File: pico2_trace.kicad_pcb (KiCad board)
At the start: 2 copper layers, 110 x 78 mm, 57 parts, among them J1B BREAKOUT, J2B BREAKOUT, J3 MIPI-20, J4 JST-SH-3 DEBUG, J5 USB-A HOST, J6 CORTEX-10, J7 JST-SH-3 DEBUG_PROBE, J8 USB-MICROB PWR, J9 USB-MICROB DEV, SW1 RESET

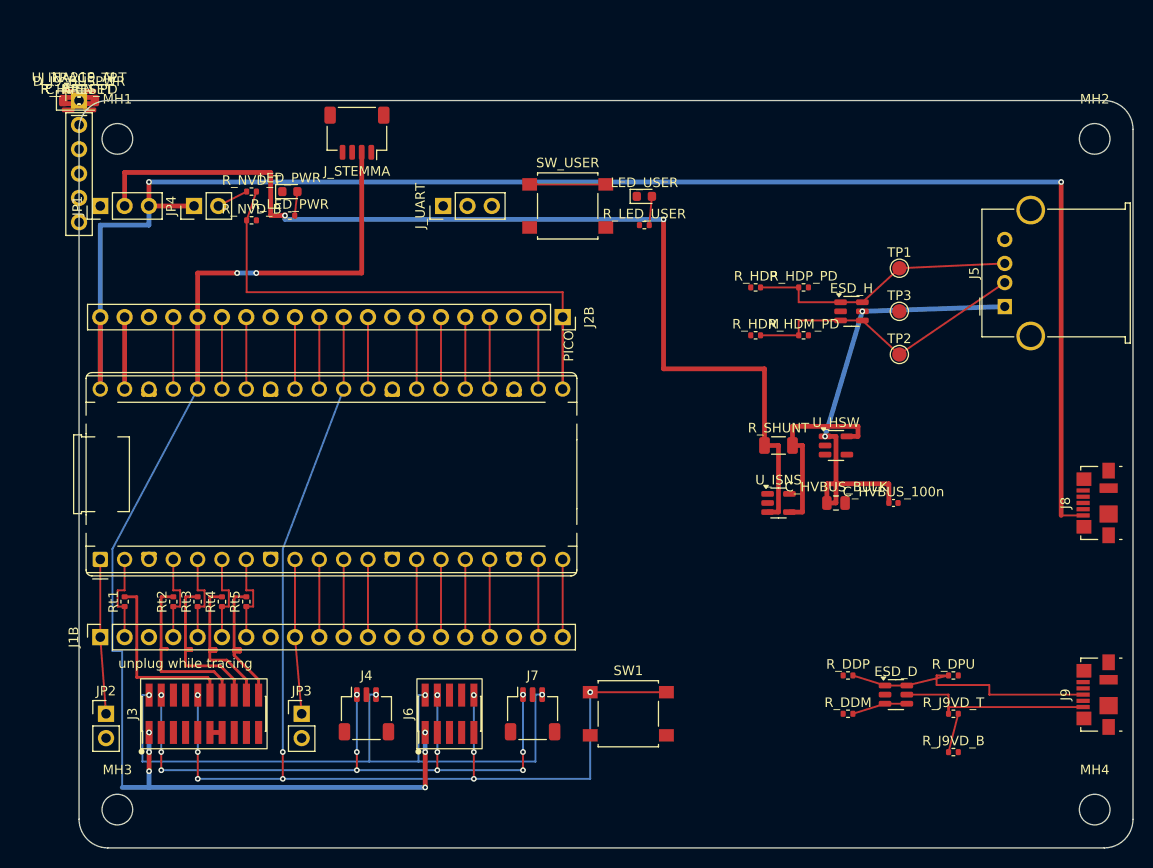
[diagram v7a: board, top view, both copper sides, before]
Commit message: WIP(14c): compact to 92x64, co-designed placement, routing rewrite
Gates NOT verified/green: silk noise 80 (target ~35), J_TRACE_TP removal
pending, full gate battery unrun. Preserved because the placement ordering
and route_trace.py band/corridor structure are reusable by the SMT-footprint
re-layout (Task 14e). Non-GND unconnected had reached 0 before the pass ended.
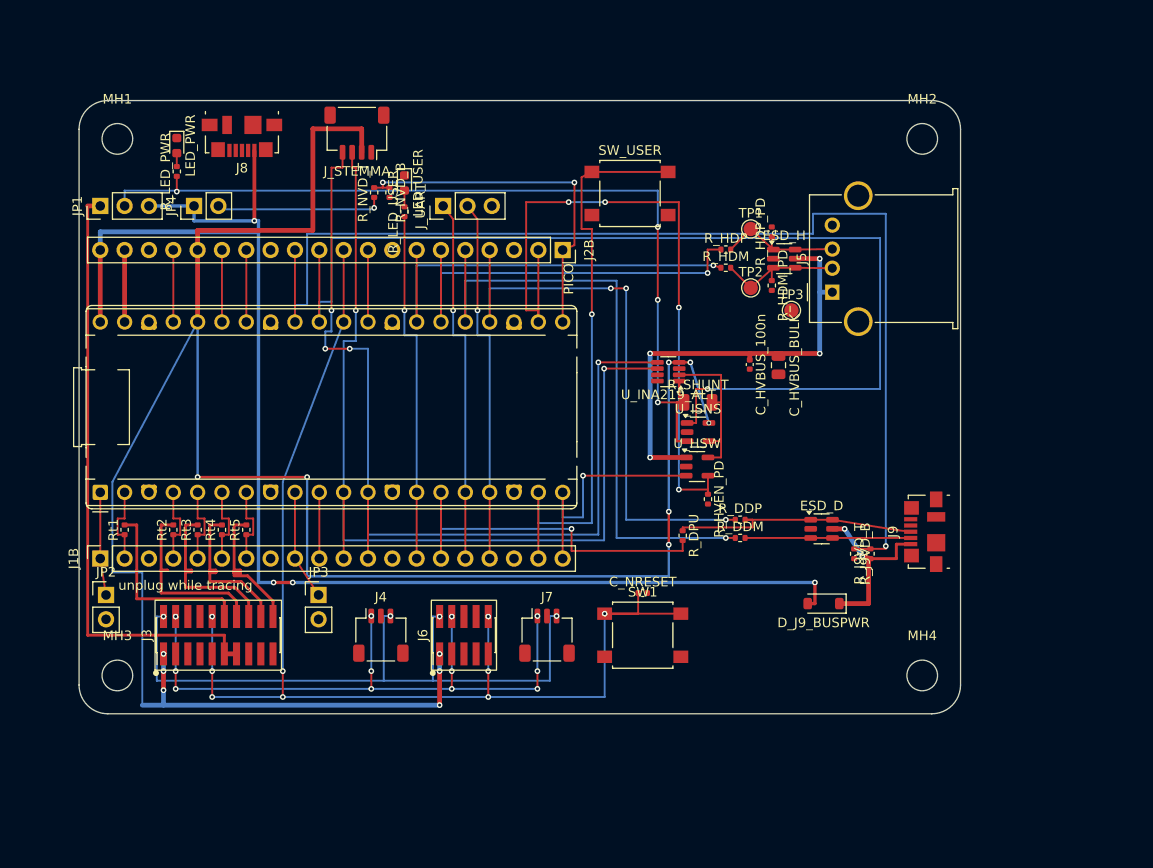
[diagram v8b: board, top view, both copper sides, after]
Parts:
- removed J_TRACE_TP: TRACE_TP, PinHeader_1x06_P2.54mm_Vertical
- moved J8 97.1 mm to (17.0, 3.75), turned to 180 degrees
- moved D_J9_BUSPWR 93.8 mm to (77.7, 52.5), turned to 180 degrees
- moved C_NRESET 78.1 mm to (58.8, 51.4)
- moved R_HVEN_PD 77.7 mm to (65.6, 41.6), turned to -90 degrees
- moved U_INA219_ALT 67.7 mm to (61.5, 28.3), turned to 180 degrees
- moved R_DPU 31.8 mm to (63.0, 45.4), turned to -90 degrees
- moved LED_USER 25.1 mm to (34.0, 8.60), turned to -90 degrees
- moved R_LED_USER 25.1 mm to (34.0, 11.6), turned to 90 degrees
- moved J9 24.8 mm to (88.3, 45.0)
- moved R_J9VD_B 23.1 mm to (80.9, 47.3), turned to -90 degrees
- moved MH4 22.8 mm to (88.0, 60.0)
- moved R_DDM 21.5 mm to (69.0, 45.6)
- moved C_HVBUS_100n 20.8 mm to (70.0, 27.6), turned to -90 degrees
- moved R_DDP 19.8 mm to (69.0, 43.8)
- moved ESD_D 19.0 mm to (77.5, 44.7)
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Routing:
- net DEV_VBUS_DET: track 11.6 -> 120.4 mm, vias 0 -> 1
- net ISENSE: track 7.51 -> 114.2 mm, vias 0 -> 1
- net P3V3: track 129.8 -> 233.0 mm, vias 8 -> 13
- net I2C0_SCL: track 8.11 -> 101.2 mm, vias 0 -> 4
- net I2C0_SDA: track 8.11 -> 99.7 mm, vias 0 -> 2
- net HOST_VBUS_EN: track 7.51 -> 72.2 mm, vias 0 -> 4
- net V5_JTRACE: track 1.27 -> 63.6 mm
- net GP19: track 7.51 -> 66.8 mm, vias 0 -> 1
- net GP18: track 7.51 -> 60.8 mm, vias 0 -> 3
- net BTN_USER: track 16.1 -> 62.0 mm, vias 0 -> 1
- net GP21: track 7.51 -> 45.2 mm, vias 0 -> 1
- net GP20: track 7.51 -> 44.3 mm, vias 0 -> 1
- net DEV_DP_PU_EN: track 8.11 -> 39.3 mm, vias 0 -> 1
- net UART0_TX: track 8.11 -> 38.4 mm, vias 0 -> 1
- net UART0_RX: track 8.11 -> 38.4 mm, vias 0 -> 1
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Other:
- board size 110 x 78 mm -> 92 x 64 mm
